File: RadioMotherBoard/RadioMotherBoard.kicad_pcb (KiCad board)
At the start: 4 copper layers, 83.8 x 36.3 mm, 103 parts, among them J1 RBUS, J10 Conn_01x01_Pin, J11 Conn_01x01_Pin, J12 Conn_01x01_Pin, J13 Conn_01x01_Pin, J14 Conn_01x01_Pin, J15 Conn_01x01_Pin, J16 Conn_01x01_Pin, J17 Conn_01x01_Pin, J18 USB_C_Receptacle_USB2.0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

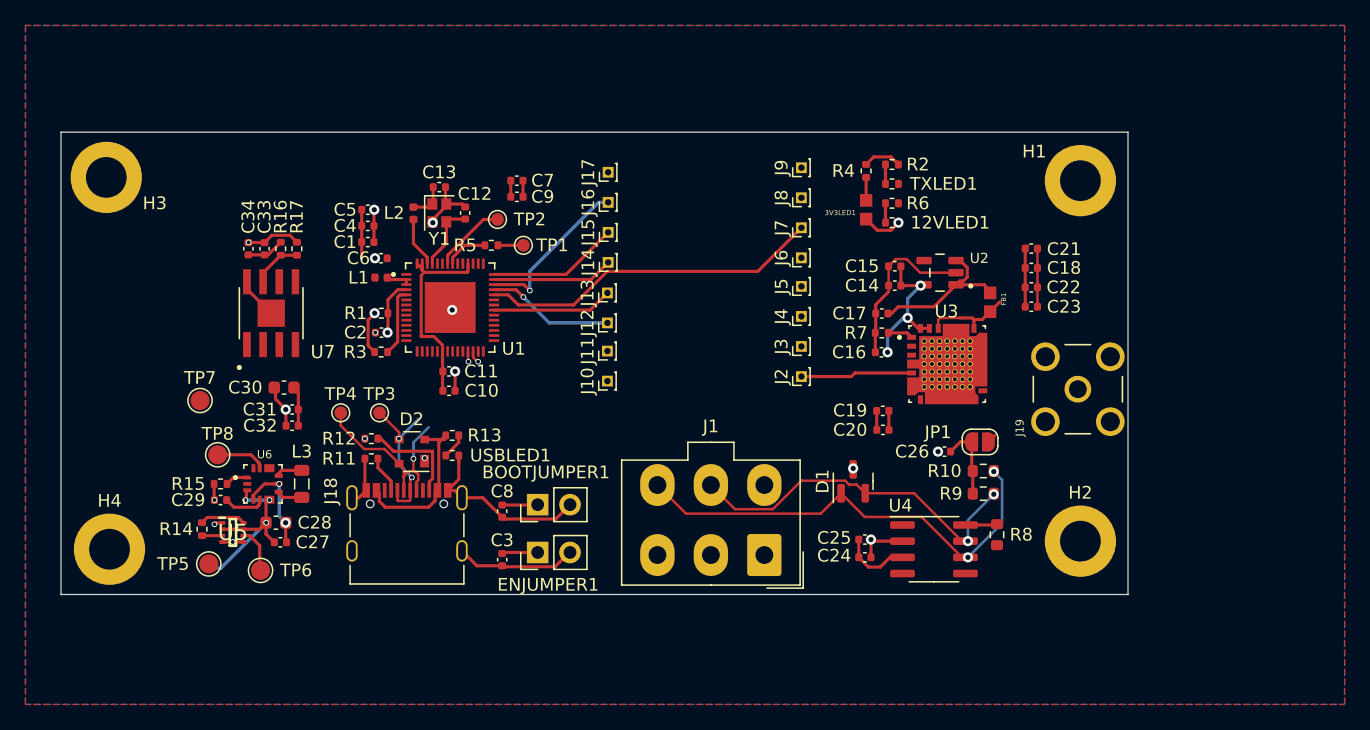
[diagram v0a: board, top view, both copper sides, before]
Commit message: Added 50 ohm lines
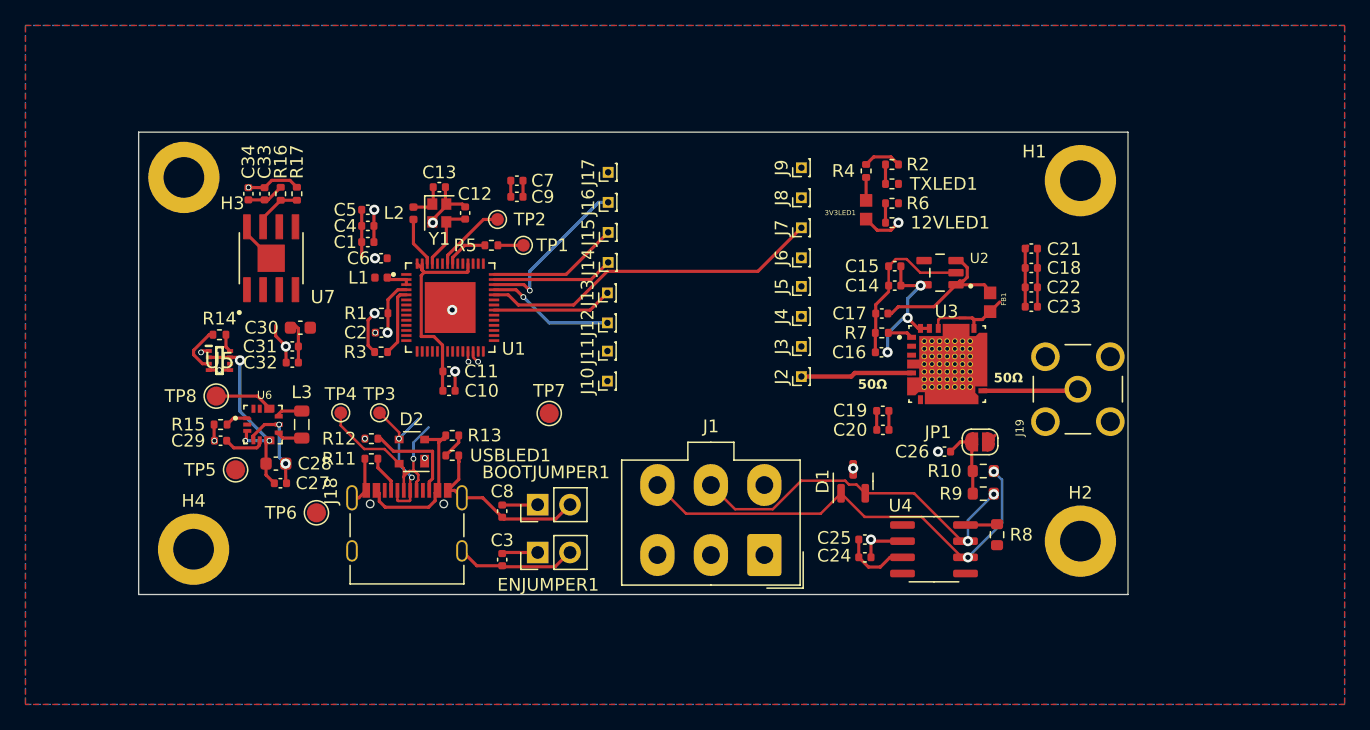
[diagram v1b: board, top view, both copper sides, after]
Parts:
- moved TP7 27.5 mm to (93.0, 136.3)
- moved R14 15.3 mm to (67.1, 130.1), turned to 0 degrees
- moved U5 13.5 mm to (67.1, 132.2)
- moved TP5 7.69 mm to (68.3, 140.7)
- moved H4 6.60 mm to (65.0, 147.0)
- moved TP6 6.31 mm to (74.7, 144.1)
- moved H3 6.10 mm to (64.3, 117.8)
- moved C31 4.96 mm to (72.8, 131.0)
- moved C32 4.96 mm to (72.8, 132.3)
- moved C30 4.87 mm to (73.4, 129.6)
- moved C29 4.66 mm to (67.1, 138.5)
- moved L3 4.66 mm to (73.5, 137.2)
- moved R15 4.66 mm to (67.1, 137.2)
- moved U6 4.66 mm to (70.5, 137.2)
- moved C27 4.64 mm to (71.8, 141.8)
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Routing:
- net Net-(U3-ANT): track 0.00 -> 7.52 mm
- net RBUS_uC_V: track 3.51 -> 0.16 mm
- net VBUS: track 14.5 -> 16.8 mm
- net Net-(U5-ST): track 3.61 -> 1.41 mm
- net /Power/BBOUT: track 6.95 -> 7.65 mm
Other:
- board size 83.8 x 36.3 mm -> 77.7 x 36.3 mm
- board text added: "50Ω"

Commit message: Board rearrange
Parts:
- moved C34 8.35 mm to (66.5, 126.9), turned to 0 degrees
- moved C33 7.75 mm to (66.5, 125.7), turned to 0 degrees
- moved R17 7.74 mm to (66.5, 123.1), turned to 180 degrees
- moved R16 7.53 mm to (66.5, 124.4), turned to 0 degrees
- moved R11 1.43 mm to (79.9, 138.8)
- moved R13 1.43 mm to (86.3, 137.0)
- moved D2 1.43 mm to (83.1, 138.2)
- moved R12 1.43 mm to (79.9, 137.2)
- moved TP3 1.43 mm to (80.6, 135.2)
- moved TP4 1.43 mm to (77.5, 135.2)
- moved USBLED1 1.43 mm to (86.3, 138.5)
- moved J13 1.05 mm to (97.3, 127.9)
- moved J14 1.05 mm to (97.3, 125.5)
- moved J15 1.05 mm to (97.3, 123.1)
- moved J16 1.05 mm to (97.3, 120.7)
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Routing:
- net /Data+: track 16.8 -> 23.4 mm
- net /Data-: track 12.9 -> 18.4 mm
- net VBUS: track 16.8 -> 12.4 mm
- net /Power/FBIn: track 3.93 -> 7.49 mm
- net GND: track 88.2 -> 91.3 mm
- net Net-(J18-CC2): track 7.89 -> 9.36 mm
- net MISO: track 12.9 -> 11.8 mm
- net /BOOT: track 8.20 -> 9.01 mm
- net Net-(J18-CC1): track 2.92 -> 3.61 mm
- net SCK: track 9.52 -> 8.85 mm
- net MOSI: track 10.3 -> 9.66 mm
- net CS: track 9.47 -> 8.80 mm
- net INT: track 27.0 -> 26.3 mm
- net TR: track 8.77 -> 9.44 mm
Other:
- outline, holes or cut-outs redrawn
